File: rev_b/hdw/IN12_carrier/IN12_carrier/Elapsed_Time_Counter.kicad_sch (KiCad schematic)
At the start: 13 parts, among them U1302 LTC4316DD

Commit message: updated footprints, ran some DRC
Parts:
- C? (x2): Digi-Key PN 311-1344-1-ND -> (none)
- C? (x3): Digi-Key PN 490-14372-1-ND -> (none)
- R1304: Digi-Key PN 311-1.00MHRCT-ND -> (none)
- R?: Digi-Key PN 311-392KHRCT-ND -> (none)
- R? (x2): Digi-Key PN RMCF0603FT10K0CT-ND -> (none)
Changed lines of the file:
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@@
       (effects (font (size 1.27 1.27)) (justify right))
     )
-    (property "Digi-Key PN" "311-1344-1-ND" (at 97.79 72.39 0)
+    (property "Digi-Key PN" "" (at 97.79 72.39 0)
       (effects (font (size 1.27 1.27)) hide)
     )
@@
       (effects (font (size 1.27 1.27)) hide)
     )
-    (property "Digi-Key PN" "490-14372-1-ND" (at 59.055 59.69 0)
+    (property "Digi-Key PN" "" (at 59.055 59.69 0)
       (effects (font (size 1.524 1.524)) hide)
     )
@@
       (effects (font (size 1.27 1.27)))
     )
-    (property "Digi-Key PN" "311-1.00MHRCT-ND" (at 208.28 123.19 0)
+    (property "Digi-Key PN" "" (at 208.28 123.19 0)
       (effects (font (size 1.524 1.524)) hide)
     )
@@
       (effects (font (size 1.27 1.27)) (justify left))
     )
-    (property "Digi-Key PN" "311-392KHRCT-ND" (at 181.61 120.65 0)
+    (property "Digi-Key PN" "" (at 181.61 120.65 0)
       (effects (font (size 1.27 1.27)) hide)
     )
@@
       (effects (font (size 1.27 1.27)) hide)
     )
-    (property "Digi-Key PN" "490-14372-1-ND" (at 92.075 59.69 0)
+    (property "Digi-Key PN" "" (at 92.075 59.69 0)
       (effects (font (size 1.524 1.524)) hide)
     )
@@
       (effects (font (size 1.27 1.27)) hide)
     )
-    (property "Digi-Key PN" "490-14372-1-ND" (at 75.565 59.69 0)
+    (property "Digi-Key PN" "" (at 75.565 59.69 0)
       (effects (font (size 1.524 1.524)) hide)
     )
@@
       (effects (font (size 1.27 1.27)) (justify left))
     )
-    (property "Digi-Key PN" "RMCF0603FT10K0CT-ND" (at 139.7 82.55 0)
+    (property "Digi-Key PN" "" (at 139.7 82.55 0)
       (effects (font (size 1.524 1.524)) hide)
     )
@@
       (effects (font (size 1.27 1.27)) (justify right))
     )
-    (property "Digi-Key PN" "311-1344-1-ND" (at 160.02 72.39 0)
+    (property "Digi-Key PN" "" (at 160.02 72.39 0)
       (effects (font (size 1.27 1.27)) hide)
     )
@@
       (effects (font (size 1.27 1.27)) (justify left))
     )
-    (property "Digi-Key PN" "RMCF0603FT10K0CT-ND" (at 127 82.55 0)
-      (effects (font (size 1.524 1.524)) hide)
-    )
+    (property "Digi-Key PN" "" (at 127 82.55 0)
+      (effects (font (size 1.524 1.524)) hide)
+    )

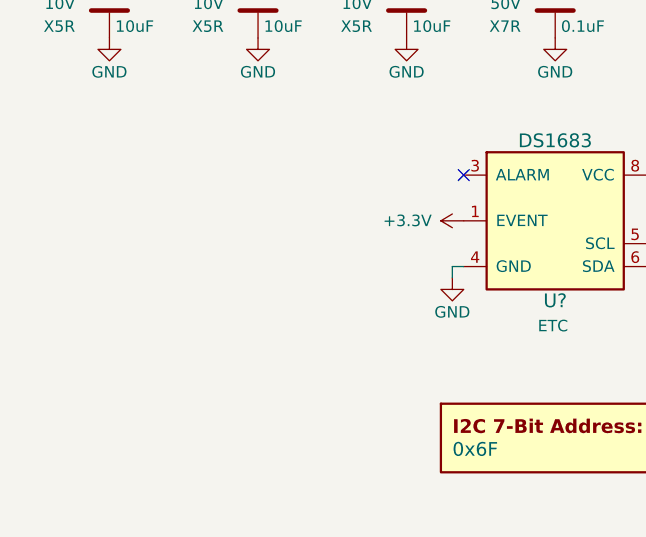
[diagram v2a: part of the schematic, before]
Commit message: added BOM for IN12 carrier, finished routing, some schematic tweaks, adjusted design rules for ERC
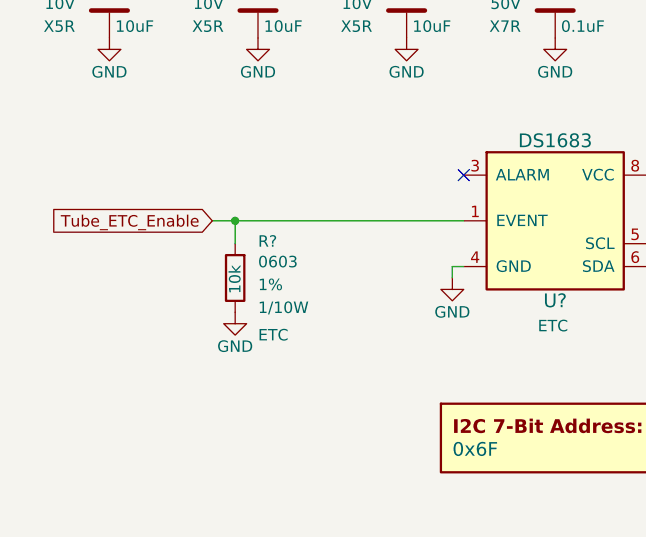
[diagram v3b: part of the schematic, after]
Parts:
- added R?: 10k, Resistors_SMD:R_0603, symbol Custom_Library:R_Custom
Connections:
- net +3.3V: no longer U?.1 (EVENT)
- net GND: now also R?.2
- new net Tube_ETC_Enable: R?.1, U?.1 (EVENT)
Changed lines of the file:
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@@
     (company "Drew Maatman")
+  )
+  (junction (at 62.23 96.52) (diameter 0) (color 0 0 0 0)
   )
   (junction (at 64.77 66.04) (diameter 0) (color 0 0 0 0)
@@
   (no_connect (at 146.05 92.71))
   (no_connect (at 87.63 91.44))
+  (wire (pts (xy 87.63 96.52) (xy 62.23 96.52))
+    (stroke (width 0) (type default))
+  )
   (wire (pts (xy 48.26 63.5) (xy 48.26 66.04))
     (stroke (width 0) (type default))
@@
     (stroke (width 0) (type default))
   )
+  (wire (pts (xy 59.69 96.52) (xy 62.23 96.52))
+    (stroke (width 0) (type default))
+  )
   (wire (pts (xy 194.31 115.57) (xy 181.61 115.57))
     (stroke (width 0) (type default))
@@
   )
   (wire (pts (xy 110.49 91.44) (xy 107.95 91.44))
+    (stroke (width 0) (type default))
+  )
+  (wire (pts (xy 62.23 96.52) (xy 62.23 99.06))
     (stroke (width 0) (type default))
   )
@@
     (effects (font (size 1.27 1.27)) (justify left))
     (property "Intersheetrefs" "${INTERSHEET_REFS}" (at 186.69 99.06 0)
+      (effects (font (size 1.27 1.27)) hide)
+    )
+  )
+  (global_label "Tube_ETC_Enable" (shape input) (at 59.69 96.52 180)
+    (effects (font (size 1.27 1.27)) (justify right))
+    (property "Intersheetrefs" "${INTERSHEET_REFS}" (at 59.69 96.52 0)
       (effects (font (size 1.27 1.27)) hide)
     )
@@
     )
   )
+  (symbol (lib_id "Custom_Library:R_Custom") (at 62.23 102.87 0) (unit 1)
+    (in_bom yes) (on_board yes) (dnp no)
+    (property "Reference" "R?" (at 64.77 98.806 0)
+      (effects (font (size 1.27 1.27)) (justify left))
+    )
+    (property "Value" "10k" (at 62.23 104.648 90)
+      (effects (font (size 1.27 1.27)) (justify left))
+    )
+    (property "Footprint" "Resistors_SMD:R_0603" (at 62.23 102.87 0)
+      (effects (font (size 1.27 1.27)) hide)
+    )
+    (property "Datasheet" "" (at 62.23 102.87 0)
+      (effects (font (size 1.27 1.27)))
+    )
+    (property "display_footprint" "0603" (at 64.77 101.092 0)
+      (effects (font (size 1.27 1.27)) (justify left))
+    )
+    (property "Tolerance" "1%" (at 64.77 103.632 0)
+      (effects (font (size 1.27 1.27)) (justify left))
+    )
+    (property "Wattage" "1/10W" (at 64.77 106.172 0)
+      (effects (font (size 1.27 1.27)) (justify left))
+    )
+    (property "Digi-Key PN" "" (at 69.85 92.71 0)
+      (effects (font (size 1.524 1.524)) hide)
+    )
+    (property "Configuration" "ETC" (at 64.77 109.22 0)
+      (effects (font (size 1.27 1.27)) (justify left))
+    )
+    (pin "1")
+    (pin "2")
+    (instances
+      (project "IV-6_Display_Board"
+        (path "/037cf18f-76c7-4b1d-9164-861d54e9914b/00000000-0000-0000-0000-00005d784813"
+          (reference "R?") (unit 1)
+        )
+        (path "/037cf18f-76c7-4b1d-9164-861d54e9914b/00000000-0000-0000-0000-00005e28cfdf"
+          (reference "R?") (unit 1)
+        )
+        (path "/037cf18f-76c7-4b1d-9164-861d54e9914b/00000000-0000-0000-0000-00005e3c80c8"
+          (reference "R?") (unit 1)
+        )
+        (path "/037cf18f-76c7-4b1d-9164-861d54e9914b/00000000-0000-0000-0000-00005e2a7ee3"
+          (reference "R1302") (unit 1)
+        )
+        (path "/037cf18f-76c7-4b1d-9164-861d54e9914b/00000000-0000-0000-0000-00005d739492"
+          (reference "R?") (unit 1)
+        )
+        (path "/037cf18f-76c7-4b1d-9164-861d54e9914b/00000000-0000-0000-0000-00005e3c97b4"
+          (reference "R?") (unit 1)
+        )
+        (path "/037cf18f-76c7-4b1d-9164-861d54e9914b/00000000-0000-0000-0000-00005e36ce18"
+          (reference "R?") (unit 1)
+        )
+        (path "/037cf18f-76c7-4b1d-9164-861d54e9914b/00000000-0000-0000-0000-00005d6b2673"
+          (reference "R?") (unit 1)
+        )
+      )
+      (project "IN12_carrier"
+        (path "/c4d83a5b-e6ae-4326-9df5-0c4ac01f7d8c/84500e28-af87-4d07-8059-0f12d4d45ee2"
+          (reference "R305") (unit 1)
+        )
+      )
+    )
+  )
   (symbol (lib_id "power:+3.3V") (at 160.02 68.58 0) (unit 1)
     (in_bom yes) (on_board yes) (dnp no)
@@
     )
   )
-  (symbol (lib_id "power:+3.3V") (at 87.63 96.52 90) (unit 1)
-    (in_bom yes) (on_board yes) (dnp no)
-    (property "Reference" "#PWR?" (at 91.44 96.52 0)
-      (effects (font (size 1.27 1.27)) hide)
-    )
-    (property "Value" "+3.3V" (at 84.074 96.52 90)
-      (effects (font (size 1.27 1.27)) (justify left))
-    )
-    (property "Footprint" "" (at 87.63 96.52 0)
-      (effects (font (size 1.27 1.27)) hide)
-    )
-    (property "Datasheet" "" (at 87.63 96.52 0)
-      (effects (font (size 1.27 1.27)) hide)
-    )
+  (symbol (lib_id "power:GND") (at 62.23 106.68 0) (unit 1)
+    (in_bom yes) (on_board yes) (dnp no)
+    (property "Reference" "#PWR?" (at 62.23 113.03 0)
+      (effects (font (size 1.27 1.27)) hide)
+    )
+    (property "Value" "GND" (at 62.23 110.49 0)
+      (effects (font (size 1.27 1.27)))
+    )
+    (property "Footprint" "" (at 62.23 106.68 0)
+      (effects (font (size 1.27 1.27)) hide)
+    )
+    (property "Datasheet" "" (at 62.23 106.68 0)
+      (effects (font (size 1.27 1.27)) hide)
+    )

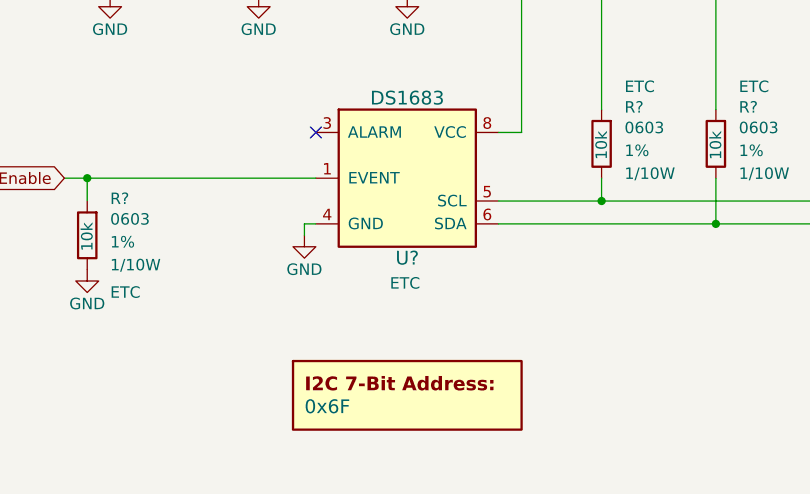
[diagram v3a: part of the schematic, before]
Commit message: assigned digikey pns to IN12 carrier board parts
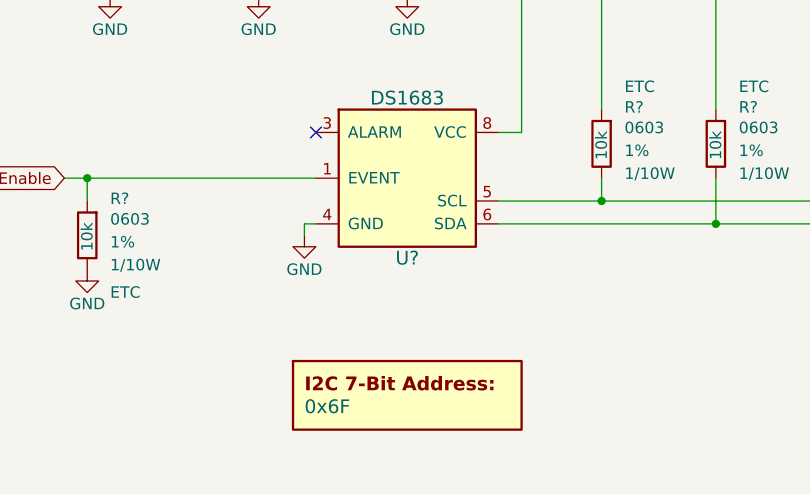
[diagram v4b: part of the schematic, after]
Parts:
- C? (x2): Digi-Key PN (none) -> 1276-CL10B104KB8NNNLCT-ND
- C? (x3): Digi-Key PN (none) -> 1276-1871-1-ND
- D?: Digi-Key PN (none) -> 497-5711-1-ND
- R1304: Digi-Key PN (none) -> 541-2990-1-ND
- R?: Digi-Key PN (none) -> 541-392KHCT-ND
- R? (x3): Digi-Key PN (none) -> 541-10.0KHCT-ND
- U?: Config ETC -> (none); Configuration (none) -> ETC
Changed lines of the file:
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@@
       (effects (font (size 1.27 1.27)) (justify right))
     )
-    (property "Digi-Key PN" "" (at 97.79 72.39 0)
+    (property "Digi-Key PN" "1276-CL10B104KB8NNNLCT-ND" (at 97.79 72.39 0)
       (effects (font (size 1.27 1.27)) hide)
     )
@@
       (effects (font (size 1.27 1.27)) hide)
     )
-    (property "Digi-Key PN" "" (at 59.055 59.69 0)
+    (property "Digi-Key PN" "1276-1871-1-ND" (at 59.055 59.69 0)
       (effects (font (size 1.524 1.524)) hide)
     )
@@
       (effects (font (size 1.27 1.27)))
     )
-    (property "Digi-Key PN" "" (at 208.28 123.19 0)
+    (property "Digi-Key PN" "541-2990-1-ND" (at 208.28 123.19 0)
       (effects (font (size 1.524 1.524)) hide)
     )
@@
       (effects (font (size 1.27 1.27)) (justify left))
     )
-    (property "Digi-Key PN" "" (at 181.61 120.65 0)
+    (property "Digi-Key PN" "541-392KHCT-ND" (at 181.61 120.65 0)
       (effects (font (size 1.27 1.27)) hide)
     )
@@
       (effects (font (size 1.27 1.27)) hide)
     )
-    (property "Digi-Key PN" "" (at 92.075 59.69 0)
+    (property "Digi-Key PN" "1276-1871-1-ND" (at 92.075 59.69 0)
       (effects (font (size 1.524 1.524)) hide)
     )
@@
       (effects (font (size 1.27 1.27)) (justify left))
     )
-    (property "Digi-Key PN" "" (at 69.85 92.71 0)
+    (property "Digi-Key PN" "541-10.0KHCT-ND" (at 69.85 92.71 0)
       (effects (font (size 1.524 1.524)) hide)
     )
@@
       (effects (font (size 1.27 1.27)) hide)
     )
-    (property "Digi-Key PN" "" (at 75.565 59.69 0)
+    (property "Digi-Key PN" "1276-1871-1-ND" (at 75.565 59.69 0)
       (effects (font (size 1.524 1.524)) hide)
     )
@@
       (effects (font (size 1.524 1.524)) hide)
     )
-    (property "Config" "ETC" (at 97.536 108.204 0)
-      (effects (font (size 1.27 1.27)))
+    (property "Config" "" (at 97.536 108.204 0)
+      (effects (font (size 1.27 1.27)))
+    )
+    (property "Configuration" "ETC" (at 97.79 96.52 0)
+      (effects (font (size 1.27 1.27)) hide)
     )
     (pin "1")
@@
       (effects (font (size 1.27 1.27)) (justify right))
     )
+    (property "Digi-Key PN" "497-5711-1-ND" (at 48.26 59.69 0)
+      (effects (font (size 1.27 1.27)) hide)
+    )
     (pin "1")
     (pin "2")
@@
       (effects (font (size 1.27 1.27)) (justify left))
     )
-    (property "Digi-Key PN" "" (at 139.7 82.55 0)
+    (property "Digi-Key PN" "541-10.0KHCT-ND" (at 139.7 82.55 0)
       (effects (font (size 1.524 1.524)) hide)
     )
@@
       (effects (font (size 1.27 1.27)) (justify right))
     )
-    (property "Digi-Key PN" "" (at 160.02 72.39 0)
+    (property "Digi-Key PN" "1276-CL10B104KB8NNNLCT-ND" (at 160.02 72.39 0)
       (effects (font (size 1.27 1.27)) hide)
     )
@@
       (effects (font (size 1.27 1.27)) (justify left))
     )
-    (property "Digi-Key PN" "" (at 127 82.55 0)
-      (effects (font (size 1.524 1.524)) hide)
-    )
+    (property "Digi-Key PN" "541-10.0KHCT-ND" (at 127 82.55 0)
+      (effects (font (size 1.524 1.524)) hide)
+    )
